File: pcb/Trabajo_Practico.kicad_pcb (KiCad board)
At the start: 2 copper layers, 49 parts, among them J1 USB_B_Micro, Q1 UMH3N, SW1 SW_MEC_5G, SW2 SW_SPDT, SW3 UP, SW4 DOWN, SW5 LEFT, SW6 RIGHT, SW7 A, SW8 B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

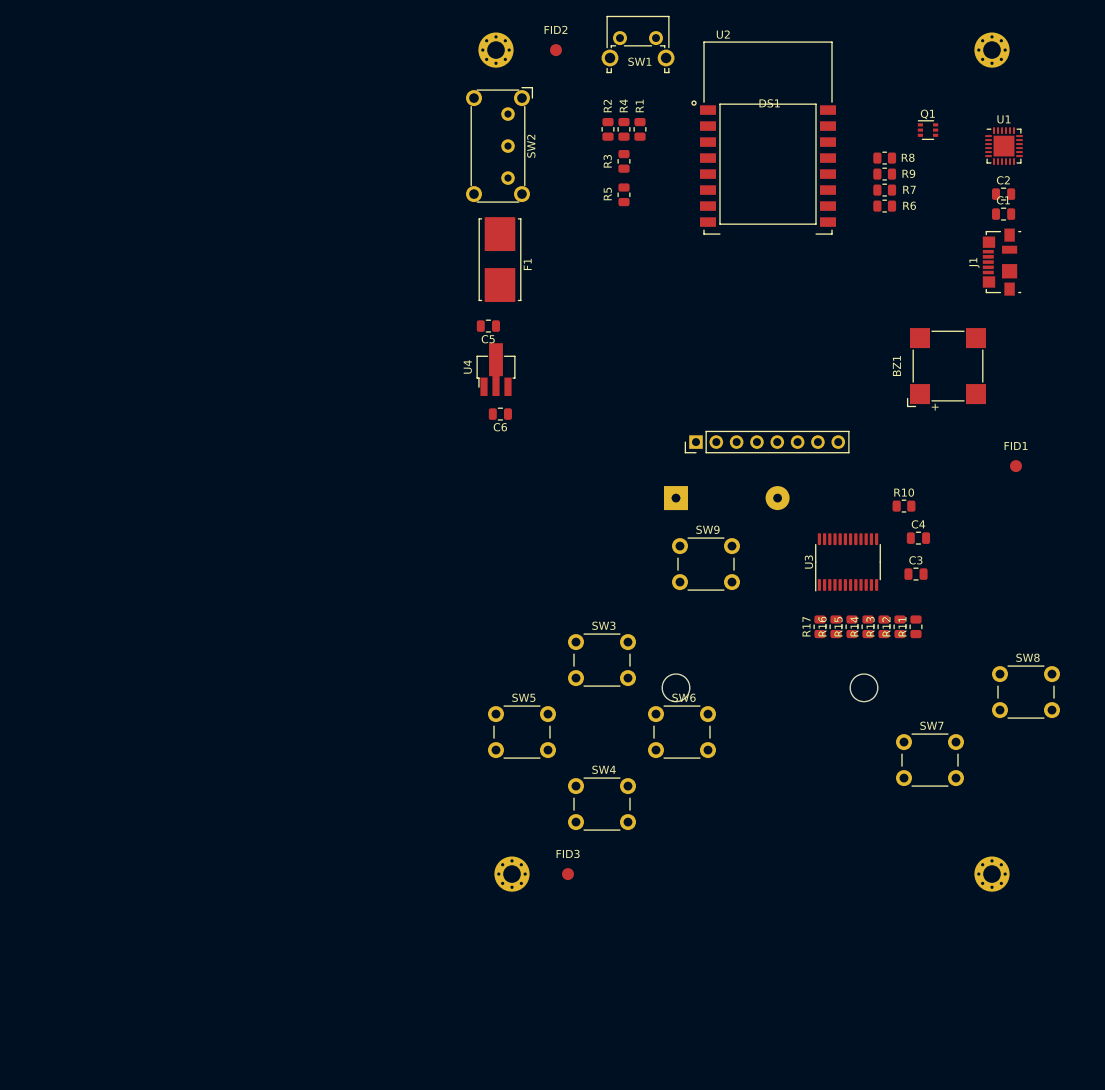
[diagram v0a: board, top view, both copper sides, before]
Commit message: Updated PCB component place and board edge
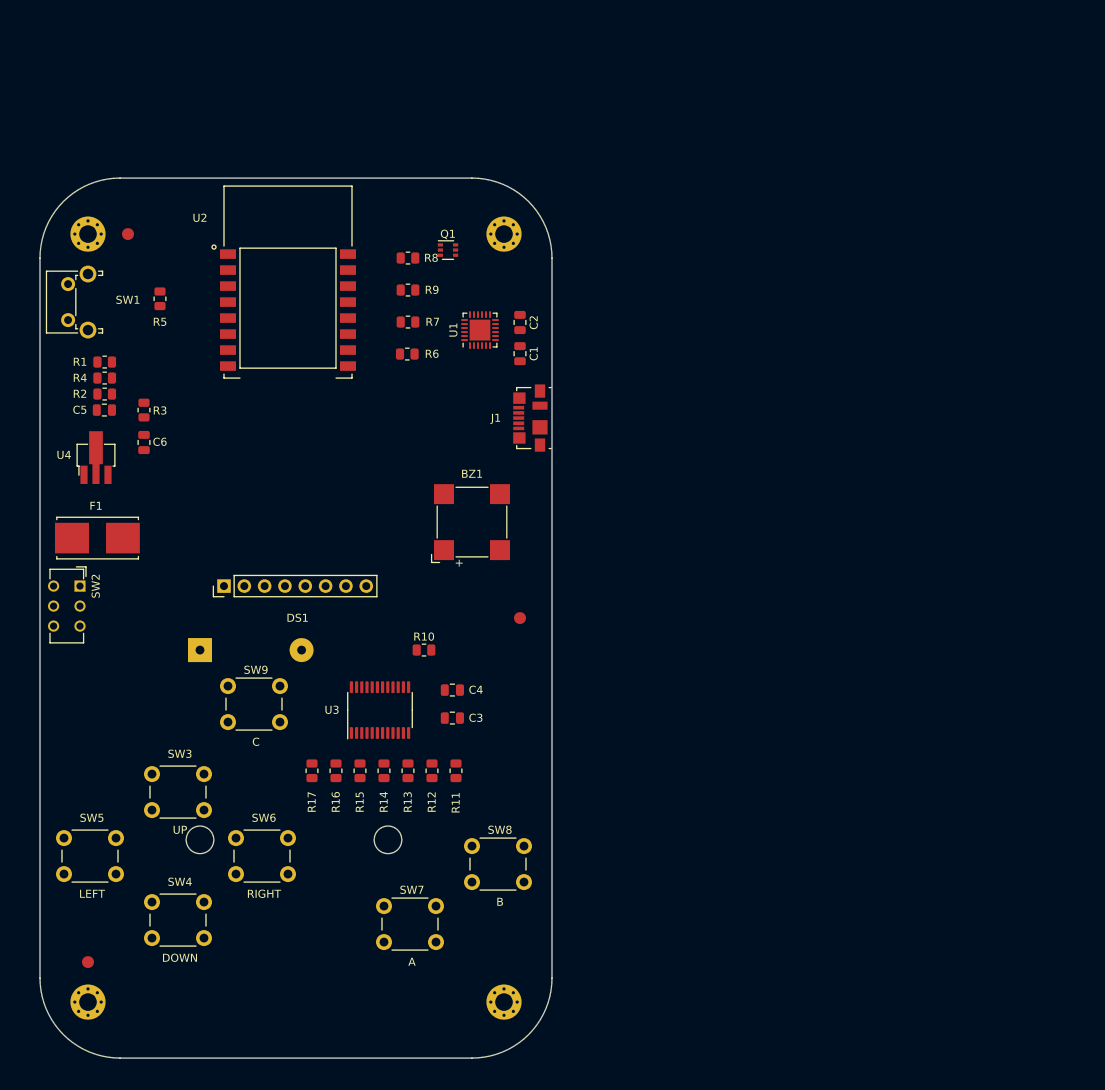
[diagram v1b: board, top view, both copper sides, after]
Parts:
- SW2: footprint Button_Switch_THT:SW_E-Switch_EG1224_SPDT_Angled -> Button_Switch_THT:SW_CuK_JS202011AQN_DPDT_Angled
- moved SW2 79.6 mm to (115.0, 90.0)
- moved SW1 77.5 mm to (113.5, 56.8), turned to 90 degrees
- moved R1 73.0 mm to (118.1, 62.0), turned to 0 degrees
- moved R4 72.0 mm to (118.1, 64.0), turned to 0 degrees
- moved R2 71.1 mm to (118.1, 66.0), turned to 0 degrees
- moved U1 69.4 mm to (165.0, 58.0), turned to 90 degrees
- moved SW8 69.4 mm to (164.0, 122.5)
- moved SW7 68.2 mm to (153.0, 130.0)
- moved R3 67.6 mm to (123.0, 68.0)
- moved R17 66.0 mm to (144.0, 113.1)
- moved F1 65.6 mm to (114.0, 84.0), turned to 0 degrees
- moved H2 65.2 mm to (168.0, 46.0)
- moved R16 65.0 mm to (147.0, 113.1)
- moved FID1 64.8 mm to (170.0, 94.0)
- moved R15 64.1 mm to (150.0, 113.1)
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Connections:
- net Net-(J1-Pad2) renamed /D-
- net Net-(J1-Pad3) renamed /D+
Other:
- board outline added: 64 x 110 mm
- net class Default: trace_width 0.25 -> 0.4; via_dia 0.8 -> 1.6; via_drill 0.4 -> 0.8
- rule pad_to_mask_clearance: 0 -> 0.4
- rule trace_min: 0.2 -> 0
- rule via_min_size: 0.4 -> 1.6
- board text added: "Grid: - 1mm Edge and component placement - 0.5 J1 (micro-USB)"

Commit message: modified switch to SMD
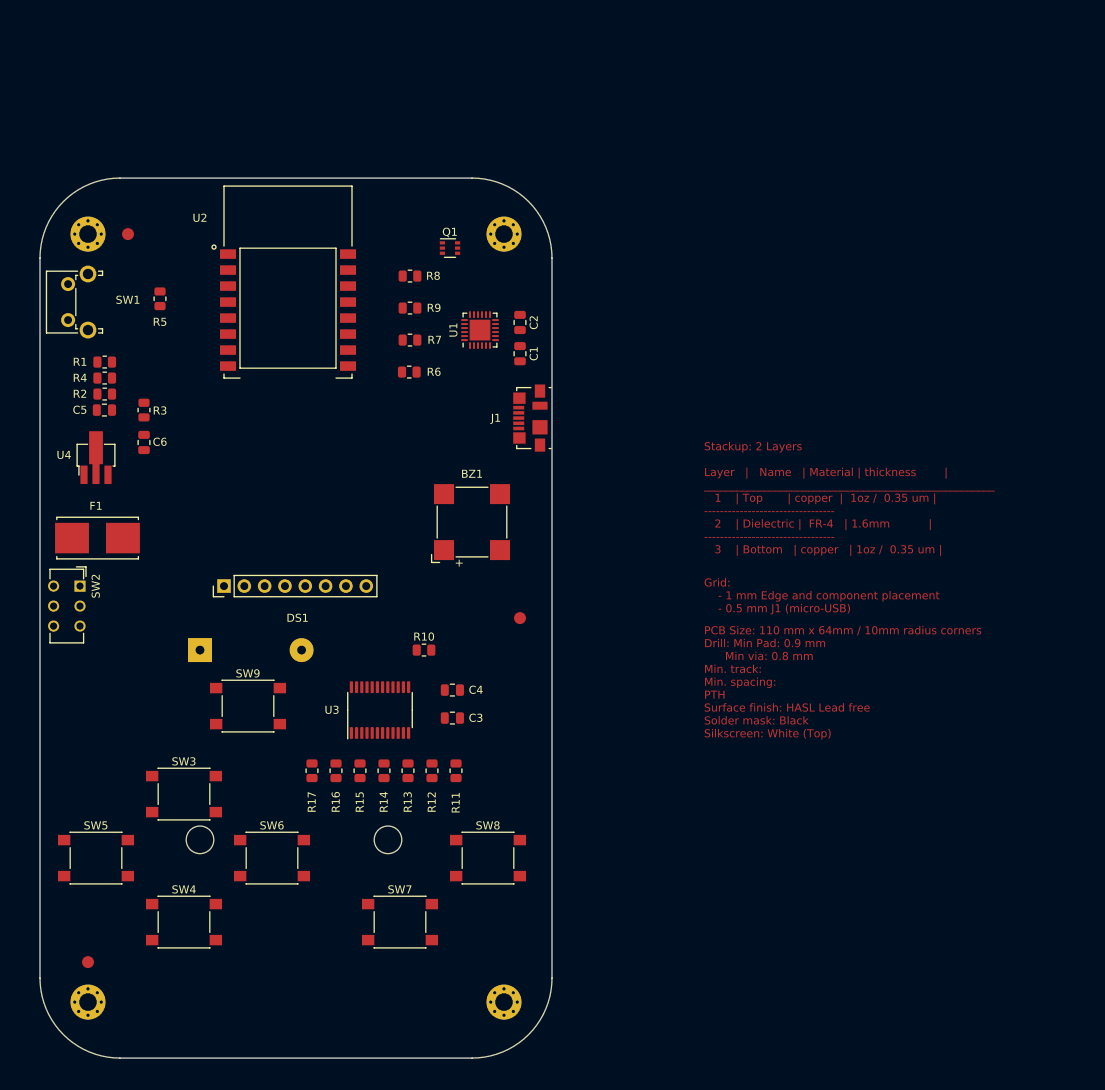
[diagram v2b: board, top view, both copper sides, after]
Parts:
- SW3, SW4, SW5, SW6, SW7, SW8, SW9: footprint TP_Footprints:SW_PUSH_6mm_H4.3mm -> Button_Switch_SMD:SW_SPST_PTS645
- moved SW6 5.15 mm to (139.0, 124.0)
- moved SW3 4.72 mm to (128.0, 116.0)
- moved SW4 4.72 mm to (128.0, 132.0)
- moved SW5 4.72 mm to (117.0, 124.0)
- moved SW9 3.54 mm to (136.0, 105.0)
- moved SW7 2.83 mm to (155.0, 132.0)
- moved SW8 2.50 mm to (166.0, 124.0)
- moved R6 2.26 mm to (156.2, 63.2)
- moved R7 2.26 mm to (156.2, 59.2)
- moved R8 2.26 mm to (156.2, 51.2)
- moved R9 2.26 mm to (156.2, 55.2)
- moved Q1 0.35 mm to (161.2, 47.8)
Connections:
- SW3 pad 2: Net-(R17-Pad2) -> GND
- SW4 pad 2: Net-(R16-Pad2) -> GND
- SW5 pad 2: Net-(R15-Pad2) -> GND
- SW6 pad 2: Net-(R14-Pad2) -> GND
- SW7 pad 2: Net-(R13-Pad2) -> GND
- SW8 pad 2: Net-(R12-Pad2) -> GND
- SW9 pad 2: Net-(R11-Pad2) -> GND
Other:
- rule pad_to_mask_clearance: 0.4 -> 0.3
- rule solder_mask_min_width: 0.2 -> 0.3
- board text added: "Grid: - 1 mm Edge and component placement - 0.5 mm J1 (micro-USB)"
- board text added: "PCB Size: 110 mm x 64mm / 10mm radius corners Drill: Min Pad: 0.9 mm Min via: 0.8 mm Min. track: Min. spacing: PTH Surface finish: HASL Lead free Solder mask: Black Silkscreen: White (Top)"
- board text added: "Stackup: 2 Layers Layer | Name | Material | thickness | _____________________________________________________ 1 | Top | copper | 1oz / 0.35 um | --------------------------------- 2 | Dielectric | FR-4 | 1.6mm | --------------------------------- 3 | Bottom | copper | 1oz / 0.35 um |"
- board text removed: "Grid: - 1mm Edge and component placement - 0.5 J1 (micro-USB)"

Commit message: Routed and checked
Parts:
- SW1: value SW_MEC_5G -> RESET
- moved R8 31.3 mm to (125.0, 50.0), turned to 90 degrees
- moved C3 17.6 mm to (148.0, 95.2)
- moved R10 16.9 mm to (144.0, 107.5), turned to 90 degrees
- moved C4 14.4 mm to (148.0, 98.0)
- moved R5 2.91 mm to (125.0, 57.0)
- moved R11 2.25 mm to (162.0, 115.3)
- moved R12 2.25 mm to (159.0, 115.3)
- moved R13 2.25 mm to (156.0, 115.3)
- moved R14 2.25 mm to (153.0, 115.3)
- moved R15 2.25 mm to (150.0, 115.3)
- moved R16 2.25 mm to (147.0, 115.3)
- moved R17 2.25 mm to (144.0, 115.3)
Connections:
- SW4 pad 1: Net-(R16-Pad2) -> Net-(R14-Pad2)
- SW5 pad 1: Net-(R15-Pad2) -> Net-(R16-Pad2)
- SW6 pad 1: Net-(R14-Pad2) -> Net-(R15-Pad2)
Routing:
- net VCC: track 0.00 -> 233.6 mm, vias 0 -> 15
- net GND: track 0.00 -> 116.9 mm, vias 0 -> 21
- net /TFT_RESET: track 0.00 -> 103.9 mm, vias 0 -> 2
- net Net-(U2-Pad14): track 0.00 -> 58.0 mm
- net Net-(BZ1-Pad1): track 0.00 -> 57.4 mm, vias 0 -> 2
- net Net-(U2-Pad13): track 0.00 -> 55.7 mm
- net Net-(R16-Pad2): track 0.00 -> 50.1 mm, vias 0 -> 2
- net /TFT_DC: track 0.00 -> 47.5 mm, vias 0 -> 2
- net Net-(R14-Pad2): track 0.00 -> 47.1 mm
- net /TFT_SCK: track 0.00 -> 40.8 mm
- net Net-(R11-Pad2): track 0.00 -> 39.7 mm
- net Net-(J1-Pad1): track 0.00 -> 38.5 mm, vias 0 -> 2
- net /TFT_SDA: track 0.00 -> 35.7 mm
- net Net-(R13-Pad2): track 0.00 -> 32.8 mm
- net Net-(R17-Pad2): track 0.00 -> 31.9 mm
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- added copper zone on B.Cu, net GND
- added copper zone on F.Cu, net GND
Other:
- net class usb added: clearance 0.2, trace_width 0.5, via_dia 1, via_drill 0.5
- rule trace_min: 0 -> 0.25
- rule via_min_size: 1.6 -> 1
- board text added: "+V GND"
- board text added: "1"
- board text added: "2"
- board text added: "Grid: - 1 mm Edge and component placement - 0.5 mm J1 (micro-USB) component placement - 0.25 mm routing"
- board text added: "Industria Argentina"
- board text added: "Nibble Retro"
- board text added: "OFF"
- board text added: "ON"
- board text added: "PCB Size: 110 mm x 64mm / 10mm radius corners Margin: 1mm Drill: Min Pad: 0.9 mm Min via: 0.5 mm Min. track: 0.25 mm Min. spacing: 0.2 mm PTH Surface finish: HASL Lead free Solder mask: Black Silkscreen: White (Top)"
- board text added: "Traces: - 1 mm - 0.4 mm (U3 tracks) - 0.25 mm (U1 tracks)"
- board text added: "USB Coupled coplanar waveguide: Width: 0.5 mm Gap: 0.2 mm Clereance: 0.2 mm"
- board text added: "V1.0.0"
- board text added: "Vias: - 1.6 mm / 0.8 mm - 1 mm / 0.5 mm (only USB D+ D- pair)"
- board text removed: "Grid: - 1 mm Edge and component placement - 0.5 mm J1 (micro-USB)"
- board text removed: "PCB Size: 110 mm x 64mm / 10mm radius corners Drill: Min Pad: 0.9 mm Min via: 0.8 mm Min. track: Min. spacing: PTH Surface finish: HASL Lead free Solder mask: Black Silkscreen: White (Top)"
